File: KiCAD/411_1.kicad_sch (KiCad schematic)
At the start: 12 parts

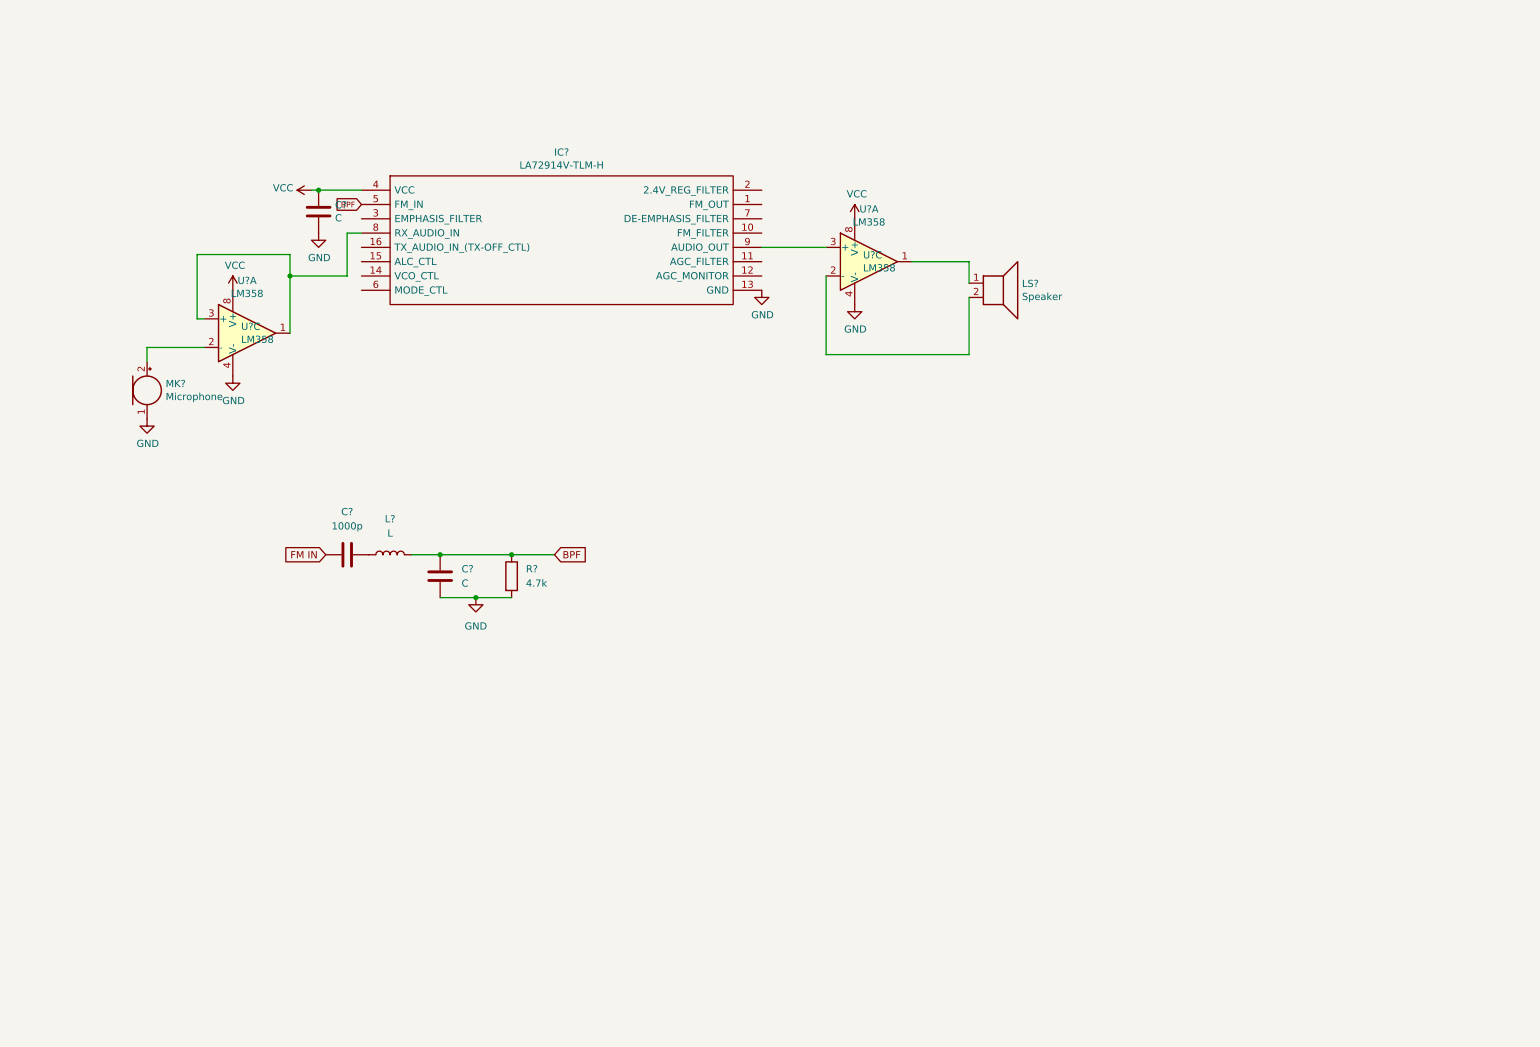
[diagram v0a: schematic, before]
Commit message: Updated schematic with all of the things.  Started preliminary layout
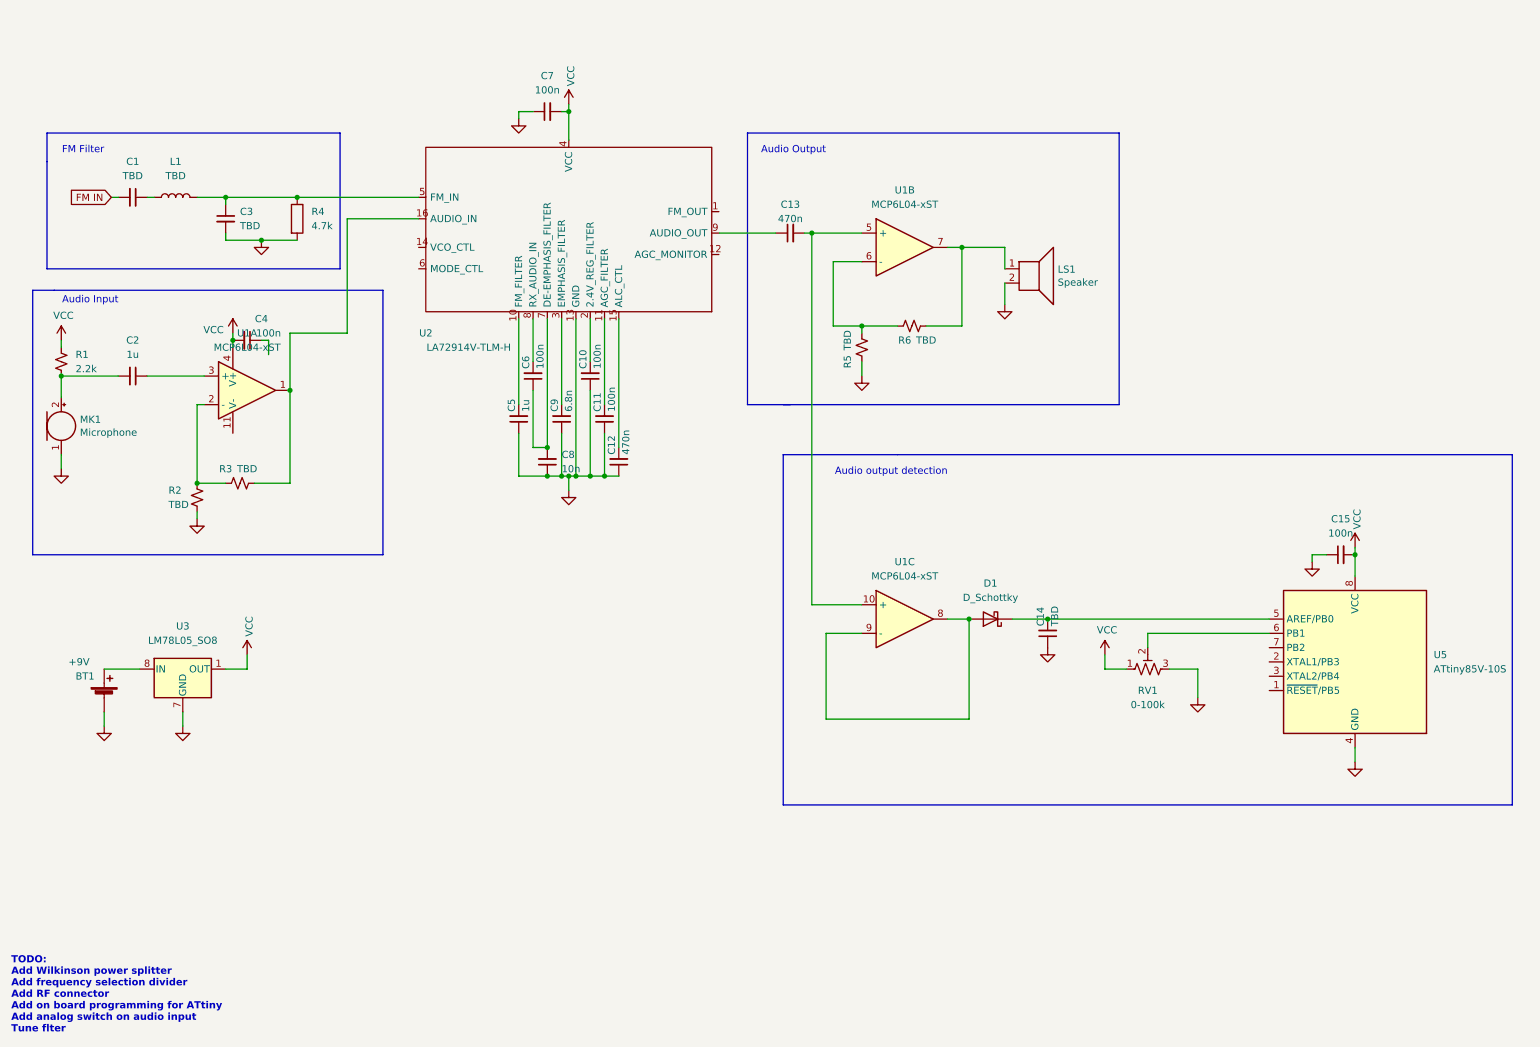
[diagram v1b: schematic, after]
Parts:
- removed C? (x2): C, symbol Device:C
- removed C?: 1000p, symbol Device:C
- removed U? (x4): LM358, symbol Amplifier_Operational:LM358
- added BT1: +9V, symbol Device:Battery_Cell
- added C1, C14, C3: TBD, Capacitor_SMD:C_0805_2012Metric, symbol Device:C_Small
- added C10, C11, C15, C4, C6, C7: 100n, Capacitor_SMD:C_0805_2012Metric, symbol Device:C_Small
- added C12, C13: 470n, Capacitor_SMD:C_0805_2012Metric, symbol Device:C_Small
- added C2, C5: 1u, Capacitor_SMD:C_0805_2012Metric, symbol Device:C_Small
- added C8: 10n, Capacitor_SMD:C_0805_2012Metric, symbol Device:C_Small
- added C9: 6.8n, Capacitor_SMD:C_0805_2012Metric, symbol Device:C_Small
- added D1: D_Schottky, Diode_SMD:D_SOD-123, symbol Device:D_Schottky
- added R1: 2.2k, Resistor_SMD:R_0805_2012Metric, symbol Device:R_Small_US
- added R2, R3, R5, R6: TBD, Resistor_SMD:R_0805_2012Metric, symbol Device:R_Small_US
- added RV1: 0-100k, symbol Device:R_Potentiometer_Trim_US
- added U1: MCP6L04-xST, Package_SO:TSSOP-14_4.4x5mm_P0.65mm, symbol Amplifier_Operational:MCP6L04-xST
- added U3: LM78L05_SO8, Package_SO:SOIC-8_3.9x4.9mm_P1.27mm, symbol Regulator_Linear:LM78L05_SO8
- added U5: ATtiny85V-10S, Package_SO:SOIC-8W_5.3x5.3mm_P1.27mm, symbol MCU_Microchip_ATtiny:ATtiny85V-10S
- L1: renamed from L?; value L -> TBD
- LS1: renamed from LS?; footprint (none) -> Connector_PinHeader_1.00mm:PinHeader_1x02_P1.00mm_Vertical
- MK1: renamed from MK?; footprint (none) -> Connector_PinHeader_1.00mm:PinHeader_1x02_P1.00mm_Vertical
- U2: renamed from IC?; footprint SOP65P640X150-16N -> Package_SO:TSSOP-16-1EP_4.4x5mm_P0.65mm; Arrow Part Number LA72914V-TLM-H -> (none); Arrow Price/Stock https://www.arrow.com/en/products/la72914v-tlm-h/on-semicon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 -> (none); Height 1.5 -> (none); Manufacturer_Name ON Semiconductor -> (none); Manufacturer_Part_Number LA72914V-TLM-H -> (none); Mouser Part Number 863-LA72914V-TLM-H -> (none); Mouser Price/Stock https://www.mouser.co.uk/ProductDetail/ON-Semiconductor/LA7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 -> (none)
- gave numbers to parts that had none: 1
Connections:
- net FM IN: now also C1.2
- net GND: now also LS1.2, BT1.2 (-), C10.1, C11.1, C12.1, C14.1, C15.1, C3.2, C5.1, C7.1, C8.1, C9.1, R2.1, R5.2, RV1.3, U3.2 (GND), U3.3 (GND), U3.6 (GND), U3.7 (GND), U5.4 (GND)
- net VCC: now also C15.2, C4.2, C7.2, R1.2, RV1.1, U1.4 (V+), U3.1 (OUT), U5.8 (VCC)
- net at LS1.1: now also R6.1, U1.7
- net at U2.9 (AUDIO_OUT): now also C13.1
- net at MK1.2 (+): now also C2.2, R1.1
- net at U2.10 (FM_FILTER): now also C5.2
- net at U2.11 (AGC_FILTER): now also C11.2
- net at U2.15 (ALC_CTL): now also C12.2
- net at U2.16 (AUDIO_IN): now also R3.1, U1.1
- net at U2.2 (2.4V_REG_FILTER): now also C10.2
- net at U2.3 (EMPHASIS_FILTER): now also C9.2
- net at U2.7 (DE-EMPHASIS_FILTER): now also C6.1, C8.2
- net at U2.8 (RX_AUDIO_IN): now also C6.2
- net at L1.1: now also C1.1
- net BPF: no longer names the net of L1.2, R4.1, U2.5 (FM_IN)
- net BPF: now also C3.1
- new net: C13.2, U1.10 (+), U1.5 (+)
- new net: D1.2 (A), U1.8, U1.9 (-)
- new net: C14.2, D1.1 (K), U5.5 (AREF/PB0)
- new net: R5.1, R6.2, U1.6 (-)
- new net: R2.2, R3.2, U1.2 (-)
- new net: C2.1, U1.3 (+)
- new net: RV1.2, U5.6 (PB1)
- new net: BT1.1 (+), U3.8 (IN)
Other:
- note added: "Audio Input"
- note added: "Audio Output"
- note added: "Audio output detection"
- note added: "FM Filter"
- note added: "TODO: Add Wilkinson power splitter Add frequency selection divider Add RF connector Add on board programming for ATtiny Add analog switch on audio input Tune flter"
- moved on the sheet: L1, LS1, MK1, R4, U2

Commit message: Add files via upload
Added two IO Signal filters, Mode Control jumper for 6.5MHz=Vcc, 4.5MHz=GND
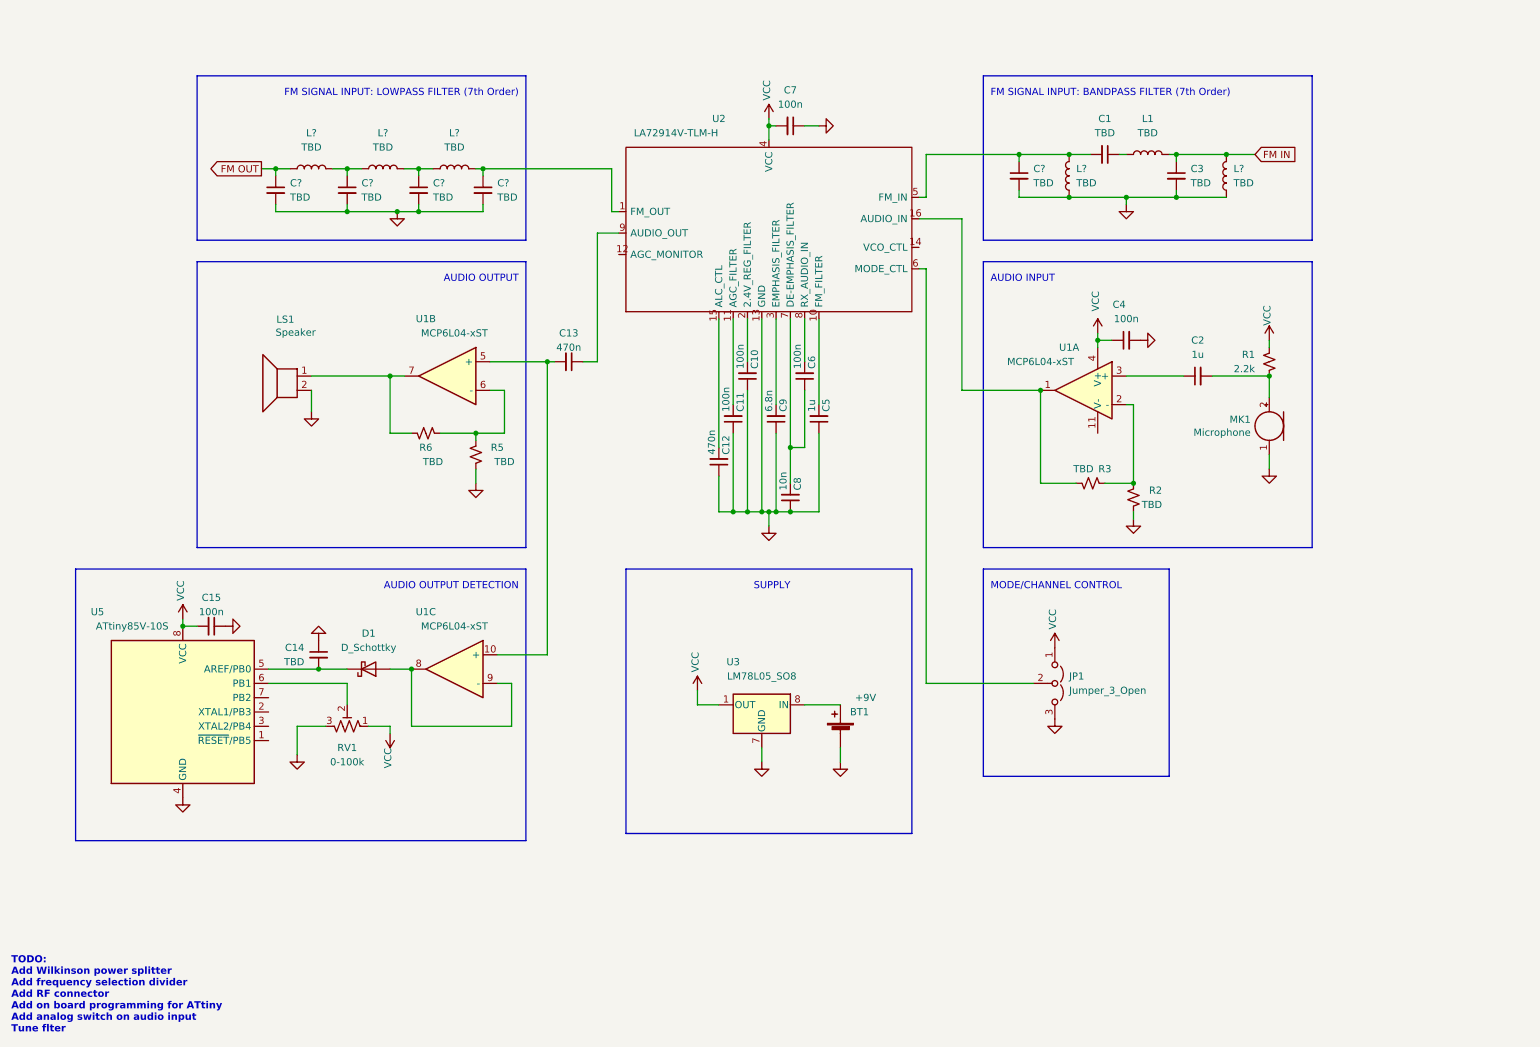
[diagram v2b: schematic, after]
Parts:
- removed R4: 4.7k, symbol Device:R
- added C? (x5): TBD, Capacitor_SMD:C_0805_2012Metric, symbol Device:C_Small
- added JP1: Jumper_3_Open, symbol Jumper:Jumper_3_Open
- added L? (x5): TBD, symbol Device:L
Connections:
- net FM IN: now also C3.1, L1.2, L?.2; no longer C1.2
- net GND: now also C4.2, C?.2, C?.2, C?.2, C?.2, C?.2, JP1.3 (B), L?.1, L?.1
- net VCC: now also C4.1, JP1.1 (A); no longer C4.2
- net at U2.1 (FM_OUT): now also C?.1, L?.2
- net at U2.6 (MODE_CTL): now also JP1.2 (C)
- new net: C1.2, C?.1, L?.2, U2.5 (FM_IN)
- new net: C?.1, L?.1, L?.2 (x2)
- new net FM OUT: C?.1, L?.1
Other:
- note added: "AUDIO INPUT"
- note added: "AUDIO OUTPUT"
- note added: "AUDIO OUTPUT DETECTION"
- note added: "FM SIGNAL INPUT: BANDPASS FILTER (7th Order)"
- note added: "FM SIGNAL INPUT: LOWPASS FILTER (7th Order)"
- note added: "MODE/CHANNEL CONTROL"
- note added: "SUPPLY"
- note removed: "Audio Input"
- note removed: "Audio Output"
- note removed: "Audio output detection"
- note removed: "FM Filter"
- company: (none) -> Portland State University
- title: (none) -> Practicum Rough Draft 
- moved on the sheet: BT1, C1, C10, C11, C12, C13, C14, C15, C2, C3, C4, C5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

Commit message: Rev 1.0 shipped to oshpark
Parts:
- removed C12, C13: 470n, Capacitor_SMD:C_0805_2012Metric, symbol Device:C_Small
- removed C5: 1u, Capacitor_SMD:C_0805_2012Metric, symbol Device:C_Small
- removed U1: MCP6L04-xST, Package_SO:TSSOP-14_4.4x5mm_P0.65mm, symbol Amplifier_Operational:MCP6L04-xST
- removed U3: LM78L05_SO8, Package_SO:SOIC-8_3.9x4.9mm_P1.27mm, symbol Regulator_Linear:LM78L05_SO8
- added C10, C18: 1u, Capacitor_THT:C_Radial_D5.0mm_H5.0mm_P2.00mm, symbol Device:C_Polarized_Small_US
- added C17: 470n, Capacitor_THT:C_Radial_D5.0mm_H5.0mm_P2.00mm, symbol Device:C_Polarized_Small_US
- added C19: 1u, Capacitor_SMD:C_0603_1608Metric_Pad1.08x0.95mm_HandSolder, symbol Device:C_Small
- added C2: 100n, Capacitor_SMD:C_0805_2012Metric_Pad1.18x1.45mm_HandSolder, symbol Device:C_Small
- added C20, C23, C4: 22u, Capacitor_SMD:C_0805_2012Metric_Pad1.18x1.45mm_HandSolder, symbol Device:C_Small
- added C7, C9: 100n, Capacitor_SMD:C_0603_1608Metric_Pad1.08x0.95mm_HandSolder, symbol Device:C_Small
- added J1, J3: Conn_Coaxial, Connector_Coaxial:U.FL_Molex_MCRF_73412-0110_Vertical, symbol Connector:Conn_Coaxial
- added J2: Conn_Coaxial, Connector_Coaxial:SMA_Amphenol_132134_Vertical, symbol Connector:Conn_Coaxial
- added J4: Conn_01x05, Connector_PinSocket_2.54mm:PinSocket_1x05_P2.54mm_Vertical, symbol Connector_Generic:Conn_01x05
- added JP2, JP3, JP4, JP5, JP6: Jumper, Jumper:SolderJumper-2_P1.3mm_Open_RoundedPad1.0x1.5mm, symbol Jumper:Jumper_2_Bridged
- added JP7: Connector_PinHeader_1.00mm:PinHeader_1x02_P1.00mm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, Connector_PinSocket_2.54mm:PinSocket_1x02_P2.54mm_Vertical, symbol Jumper:Jumper_2_Bridged
- added JP8: Jumper_2_Bridged, Connector_PinSocket_2.54mm:PinSocket_1x02_P2.54mm_Vertical, symbol Jumper:Jumper_2_Bridged
- added R10, R11, R12, R13, R4, R7, R8: 10k, Resistor_SMD:R_0603_1608Metric_Pad0.98x0.95mm_HandSolder, symbol Device:R_Small_US
- added R9: 1k, Resistor_SMD:R_0603_1608Metric_Pad0.98x0.95mm_HandSolder, symbol Device:R_Small_US
- added RV1, RV2, RV4: 0-100k, Potentiometer_SMD:Potentiometer_Bourns_3314R-1_Vertical_Hole, symbol Device:R_Potentiometer_Trim_US
- added SW1: SW_Push, Connector_PinSocket_2.54mm:PinSocket_1x02_P2.54mm_Vertical, symbol Switch:SW_Push
- added TP1, TP10, TP11, TP12, TP13, TP14, TP15, TP16, TP17, TP2, TP3, TP4, TP5, TP6, TP7, TP8, TP9: Testpoint, Connector_PinHeader_1.00mm:PinHeader_1x01_P1.00mm_Vertical, symbol Testpoint:Testpoint
- added U1: LM2937IMP, Package_TO_SOT_SMD:SOT-223-3_TabPin2, symbol Regulator_Linear:LM2937xMP
- added U2: MCP6L04x-xSL, Package_SO:SOIC-14_3.9x8.7mm_P1.27mm, symbol Amplifier_Operational:MCP6L04x-xSL
- added U3: TMUX1101, Package_TO_SOT_SMD:SOT-23-5_HandSoldering, symbol TMUX1101:TMUX1101
- BT1: footprint (none) -> Connector_JST:JST_SH_BM02B-SRSS-TB_1x02-1MP_P1.00mm_Vertical
- C1: renamed from C2; footprint Capacitor_SMD:C_0805_2012Metric -> Capacitor_SMD:C_0603_1608Metric_Pad1.08x0.95mm_HandSolder; Cost Ea (none) -> .1; DPN (none) -> 1276-1034-2-ND; Distributor (none) -> Digi-Key; MPN (none) -> CL10A105KO8NNNC
- C11: renamed from C6; footprint Capacitor_SMD:C_0805_2012Metric -> Capacitor_SMD:C_0603_1608Metric_Pad1.08x0.95mm_HandSolder; Cost Ea (none) -> .13; DPN (none) -> 399-C0603C104K4NACAUTOTR-ND; Distributor (none) -> Digi-Key; MPN (none) -> C0603C104K4NACAUTO
- C12: renamed from C7; footprint Capacitor_SMD:C_0805_2012Metric -> Capacitor_SMD:C_0603_1608Metric_Pad1.08x0.95mm_HandSolder; Cost Ea (none) -> .13; DPN (none) -> 399-C0603C104K4NACAUTOTR-ND; Distributor (none) -> Digi-Key; MPN (none) -> C0603C104K4NACAUTO
- C13: renamed from C8; footprint Capacitor_SMD:C_0805_2012Metric -> Capacitor_SMD:C_0603_1608Metric_Pad1.08x0.95mm_HandSolder; Cost Ea (none) -> .1; DPN (none) -> 1292-1386-2-ND; Distributor (none) -> Digi-Key; MPN (none) -> 0603B103K500CT
- C14: renamed from C9; footprint Capacitor_SMD:C_0805_2012Metric -> Capacitor_SMD:C_0603_1608Metric_Pad1.08x0.95mm_HandSolder; Cost Ea (none) -> .1; DPN (none) -> 1276-2099-2-ND; Distributor (none) -> Digi-Key; MPN (none) -> CL10B682JB8NNNC
- C15: renamed from C10; footprint Capacitor_SMD:C_0805_2012Metric -> Capacitor_SMD:C_0603_1608Metric_Pad1.08x0.95mm_HandSolder; Cost Ea (none) -> .13; DPN (none) -> 399-C0603C104K4NACAUTOTR-ND; Distributor (none) -> Digi-Key; MPN (none) -> C0603C104K4NACAUTO
- C16: renamed from C11; footprint Capacitor_SMD:C_0805_2012Metric -> Capacitor_SMD:C_0603_1608Metric_Pad1.08x0.95mm_HandSolder; Cost Ea (none) -> .13; DPN (none) -> 399-C0603C104K4NACAUTOTR-ND; Distributor (none) -> Digi-Key; MPN (none) -> C0603C104K4NACAUTO
- C21, C24, C25, C26: renamed from C?; value TBD -> 470p; footprint Capacitor_SMD:C_0805_2012Metric -> Capacitor_SMD:C_0603_1608Metric_Pad1.08x0.95mm_HandSolder; Cost Ea (none) -> .1; DPN (none) -> 1276-1094-2-ND; Distributor (none) -> Digi-Key; MPN (none) -> CL10B471KB8NNNC
- C22: renamed from C14; value TBD -> 22u; footprint Capacitor_SMD:C_0805_2012Metric -> Capacitor_SMD:C_0805_2012Metric_Pad1.18x1.45mm_HandSolder; Cost Ea (none) -> .4; DPN (none) -> 445-11192-2-ND; Distributor (none) -> Digi-Key; MPN (none) -> C1608JB0J226M080AC
- C27: renamed from C15; footprint Capacitor_SMD:C_0805_2012Metric -> Capacitor_SMD:C_0603_1608Metric_Pad1.08x0.95mm_HandSolder; Cost Ea (none) -> .13; DPN (none) -> 399-C0603C104K4NACAUTOTR-ND; Distributor (none) -> Digi-Key; MPN (none) -> C0603C104K4NACAUTO
- C3: renamed from C4; footprint Capacitor_SMD:C_0805_2012Metric -> Capacitor_SMD:C_0603_1608Metric_Pad1.08x0.95mm_HandSolder; Cost Ea (none) -> .13; DPN (none) -> 399-C0603C104K4NACAUTOTR-ND; Distributor (none) -> Digi-Key; MPN (none) -> C0603C104K4NACAUTO
- C5: renamed from C3; value TBD -> 5.6n; footprint Capacitor_SMD:C_0805_2012Metric -> Capacitor_SMD:C_0603_1608Metric_Pad1.08x0.95mm_HandSolder; Cost Ea (none) -> .1; DPN (none) -> 478-1224-2-ND; Distributor (none) -> Digi-Key; MPN (none) -> 06035C562KAT2A
- C6: renamed from C1; value TBD -> 5.6n; footprint Capacitor_SMD:C_0805_2012Metric -> Capacitor_SMD:C_0603_1608Metric_Pad1.08x0.95mm_HandSolder; Cost Ea (none) -> .1; DPN (none) -> 478-1224-2-ND; Distributor (none) -> Digi-Key; MPN (none) -> 06035C562KAT2A
- C8: renamed from C?; value TBD -> 5.6n; footprint Capacitor_SMD:C_0805_2012Metric -> Capacitor_SMD:C_0603_1608Metric_Pad1.08x0.95mm_HandSolder; Cost Ea (none) -> .1; DPN (none) -> 478-1224-2-ND; Distributor (none) -> Digi-Key; MPN (none) -> 06035C562KAT2A
- D1: Cost Ea (none) -> .32; DPN (none) -> MBR0580S1-7DITR-ND; Distributor (none) -> Digi-Key; MPN (none) -> MBR0580S1-7
- JP1: footprint (none) -> Jumper:SolderJumper-3_P1.3mm_Open_Pad1.0x1.5mm; DPN (none) -> 2553-2011-1X03G00SC028B-ND; Distributor (none) -> Digi-Key; MPN (none) -> 2011-1X03G00SC028B
- L1, L3: renamed from L?; value TBD -> 220n; footprint (none) -> Capacitor_SMD:C_0603_1608Metric_Pad1.08x0.95mm_HandSolder; Cost Ea (none) -> .67; DPN (none) -> 994-0603DC-R22XJRW; Distributor (none) -> Mouser; MPN (none) -> 0603DC-R22XJRW
- L2: renamed from L1; value TBD -> 220n; footprint (none) -> Capacitor_SMD:C_0603_1608Metric_Pad1.08x0.95mm_HandSolder; Cost Ea (none) -> .67; DPN (none) -> 994-0603DC-R22XJRW; Distributor (none) -> Mouser; MPN (none) -> 0603DC-R22XJRW
- L4, L5, L6: renamed from L?; value TBD -> 3.3u; footprint (none) -> Capacitor_SMD:C_0603_1608Metric_Pad1.08x0.95mm_HandSolder; Cost Ea (none) -> .54; DPN (none) -> 652-CWF1610-3R3K; Distributor (none) -> Mouser; MPN (none) -> CWF1610-3R3K
- LS1: footprint Connector_PinHeader_1.00mm:PinHeader_1x02_P1.00mm_Vertical -> Connector_PinSocket_2.54mm:PinSocket_1x02_P2.54mm_Vertical; Cost Ea (none) -> 1.95; DPN (none) -> 485-1890; Distributor (none) -> Mouser; MPN (none) -> 1890
- MK1: footprint Connector_PinHeader_1.00mm:PinHeader_1x02_P1.00mm_Vertical -> Connector_PinSocket_2.54mm:PinSocket_1x02_P2.54mm_Vertical; Cost Ea (none) -> .55; DPN (none) -> 490-CMEJ-4618-42L015; Distributor (none) -> Mouser; MPN (none) -> CMEJ-4618-42-L015
- R1: footprint Resistor_SMD:R_0805_2012Metric -> Resistor_SMD:R_0603_1608Metric_Pad0.98x0.95mm_HandSolder; Cost Ea (none) -> .10; DPN (none) -> 13-RT0603FRE132K2LTR-ND; Distributor (none) -> Digi-Key; MPN (none) -> RT0603FRE132K2L
- R2, R3, R5, R6: value TBD -> 10k; footprint Resistor_SMD:R_0805_2012Metric -> Resistor_SMD:R_0603_1608Metric_Pad0.98x0.95mm_HandSolder; Cost Ea (none) -> .10; DPN (none) -> 13-RT0603FRE132K2LTR-ND; Distributor (none) -> Digi-Key; MPN (none) -> RT0603FRE132K2L
- RV3: renamed from RV1; footprint (none) -> Potentiometer_SMD:Potentiometer_Bourns_3314R-1_Vertical_Hole; Cost Ea (none) -> 1.26; DPN (none) -> 3314R-1-104ETR-ND; Distributor (none) -> Digi-Key; MPN (none) -> 3361P-1-104GLF
- U4: renamed from U2; footprint Package_SO:TSSOP-16-1EP_4.4x5mm_P0.65mm -> Package_SO:TSSOP-16_4.4x5mm_P0.65mm; Cost Ea (none) -> 7.01; DPN (none) -> 863-LA72914V-TLM-H; Distributor (none) -> Mouser; MPN (none) -> LA72914V-TLM-H
- U5: Cost Ea (none) -> $1.43; DPN (none) -> 556-ATTINY85-20SUR; Distributor (none) -> Mouser; MPN (none) -> ATTINY85-20SUR
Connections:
- net GND: now also R3.1, R6.2, C10.2, C17.2, C2.1, C20.1, C23.1, C4.1, C7.2, J1.2 (Ext), J2.2 (Ext), J3.2 (Ext), J4.5 (Pin_5), R11.2, R13.2, R4.1, R8.2, R9.1, RV1.1, RV2.1, RV4.1, SW1.1, U1.2 (GND), U2.11 (V-), U2.13 (-), U3.3 (GND); no longer JP1.3 (B), R2.1, R5.2
- net VCC: now also R2.2, R5.1, C4.2, C7.1, R10.1, R12.1, R7.1, TP2.1, U1.3 (VO), U2.12 (+), U2.4 (V+), U3.5 (VDD); no longer JP1.1 (A)
- net at LS1.1: now also RV4.3, TP15.1, U2.7; no longer R6.1
- net at C21.1, L4.2, U4.1 (FM_OUT): now also J3.1 (In), R9.2
- net at U4.10 (FM_FILTER): now also C10.1
- net at U4.12 (AGC_MONITOR): now also TP17.1
- net at U4.14 (VCO_CTL): now also TP16.1
- net at U4.15 (ALC_CTL): now also C17.1
- net at U4.16 (AUDIO_IN): now also JP2.2 (B), TP5.1; no longer R3.1
- net at C6.2, C8.1, L3.2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: now also J1.1 (In)
- net at JP1.2 (C), U4.6 (MODE_CTL): now also TP6.1
- net at U4.9 (AUDIO_OUT): now also C18.1, TP9.1
- net at D1.2 (A): now also RV2.3, TP12.1, U2.8
- net at C22.2, D1.1 (K): now also C20.2, C23.2, JP7.1 (A), R13.1, TP14.1; no longer U5.5 (AREF/PB0)
- net at R3.2: now also C1.1, R2.1, TP1.1, U2.3 (+); no longer R2.2
- net ~{RST}: now reaches U5.1 (~{RESET}/PB5)
- net ~{RST}: now also J4.4 (Pin_4)
- net at U5.2 (XTAL1/PB3): now also R12.2, SW1.2
- net MIC_EN: now reaches U5.3 (XTAL2/PB4)
- net MIC_EN: now also R4.2, TP4.1, U3.4 (SEL)
- net at RV3.2: now also JP8.1 (A), TP13.1; no longer U5.6 (PB1)
- net SCK: now reaches U5.7 (PB2)
- net SCK: now also J4.3 (Pin_3)
- net at BT1.1 (+): now also C2.2, U1.1 (VI)
- net FM IN: no longer names the net of C5.1, L1.2, L2.2
- net FM IN: now also JP3.1 (A)
- net FM OUT: no longer names the net of C26.1, L6.1
- net FM OUT: now also JP6.2 (B)
- new net: RV1.3, TP3.1, U2.1, U3.2 (S)
- new net: RV1.2, U2.2 (-)
- new net: RV4.2, U2.6 (-)
- new net: C19.1, JP4.1 (A)
- new net: C19.2, R7.2, R8.1, TP10.1, U2.10 (+)
- new net: C18.2, JP4.2 (B), JP5.1 (A)
- new net: JP1.1 (A), R5.2
- new net: JP1.3 (B), R6.1
- new net: JP5.2 (B), R10.2, R11.1, TP11.1, U2.5 (+)
- new net: C9.2, U3.1 (D)
- new net: RV2.2, U2.9 (-)
- new net: C9.1, JP2.1 (A)
- new net MISO: J4.2 (Pin_2), JP8.2 (B), U5.6 (PB1)
- new net MOSI: J4.1 (Pin_1), JP7.2 (B), U5.5 (AREF/PB0)
- new net RF_Rx: J2.1 (In), JP3.2 (B), JP6.1 (A), TP7.1, TP8.1
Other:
- note added: "Bandpass: Rx=4.5MHz | Rx=6.5MHz L1=220n | L1=47n C5=5.6n | C5=12n L2=22u | L2=4.7u C6=56p | C6=120p L3=220n | L3=47n C8=5.6n | C5=12n"
- note added: "FM SIGNAL OUTPUT: LOWPASS FILTER (7th Order)"
- note added: "Filter Values are based on programmed Rx/Tx frequency"
- note added: "Lowpass: Tx=6.5MHz | Tx=4.5MHz C21=470p | C21=470p L4=1.2u | L4=1.2u C24=1n | C24=1n L5=1.2u | L5=1.2u C25=1n | C25=1n L6=1.2u | L6=1.2u C26=470p | C26=470p"
- note added: "MODE CONTROL"
- note added: "Notes:"
- note added: "POWER"
- note added: "Pulldown = Tx @ 4.5 MHz, Rx @6.5 MHz"
- note added: "Pullup = Tx @6.5 MHz, Rx @4.5Mhz"
- note added: "See Note for Values"
- note added: "Tied according to datasheet"
- note added: "Unused OPAMP"
- note removed: "FM SIGNAL INPUT: LOWPASS FILTER (7th Order)"
- note removed: "MODE/CHANNEL CONTROL"
- note removed: "SUPPLY"
- note removed: "TODO: Add Wilkinson power splitter Add frequency selection divider Add RF connector Add on board programming for ATtiny Add analog switch on audio input Tune flter"
- title: Practicum Rough Draft  -> RF Tin Can
- moved on the sheet: BT1, C1, C11, C12, C13, C14, C15, C16, C21, C22, C24, C25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
